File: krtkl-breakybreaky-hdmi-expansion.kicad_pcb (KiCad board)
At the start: 4 copper layers, 62.2 x 19.7 mm, 37 parts, among them J1 SMH-120-02-T-D, J2 685119134923, J3 solder_jumper, Q1 BSS138AKA, Q2 BSS138AKA, Q3 BSS138AKA, U1 TPD12S016PWR, U2 TPS61232DRCT

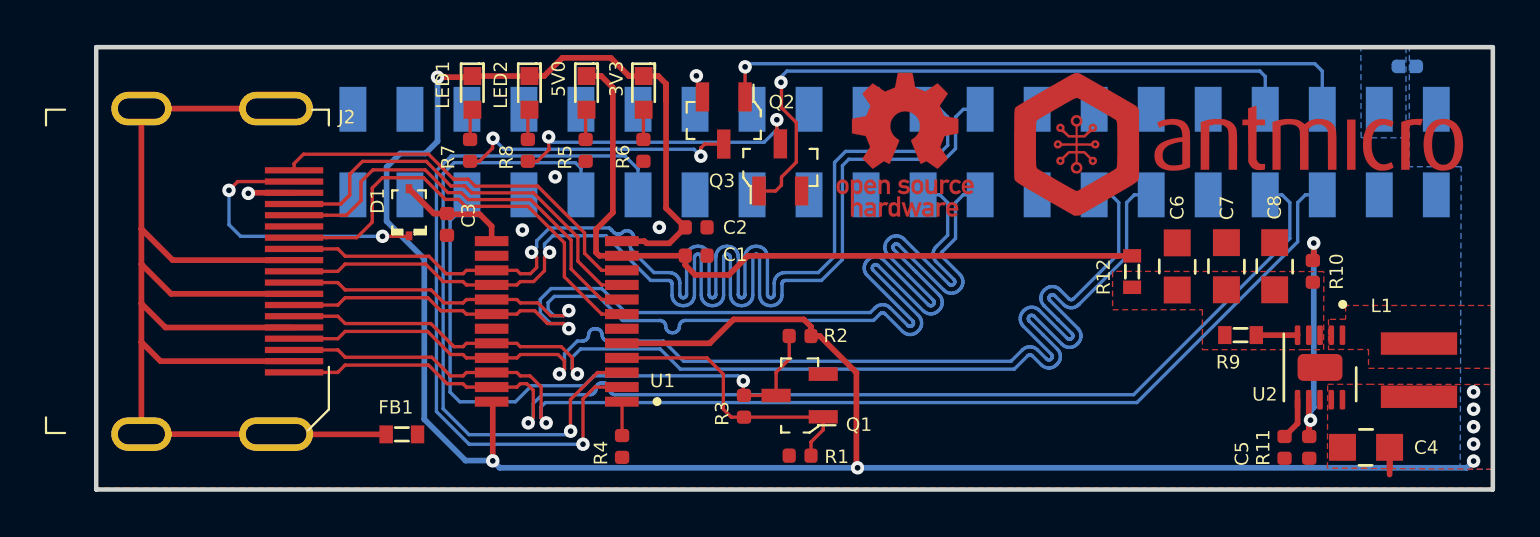
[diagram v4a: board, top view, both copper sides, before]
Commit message: Added testpads, 0R on EDID and board branding to PCB
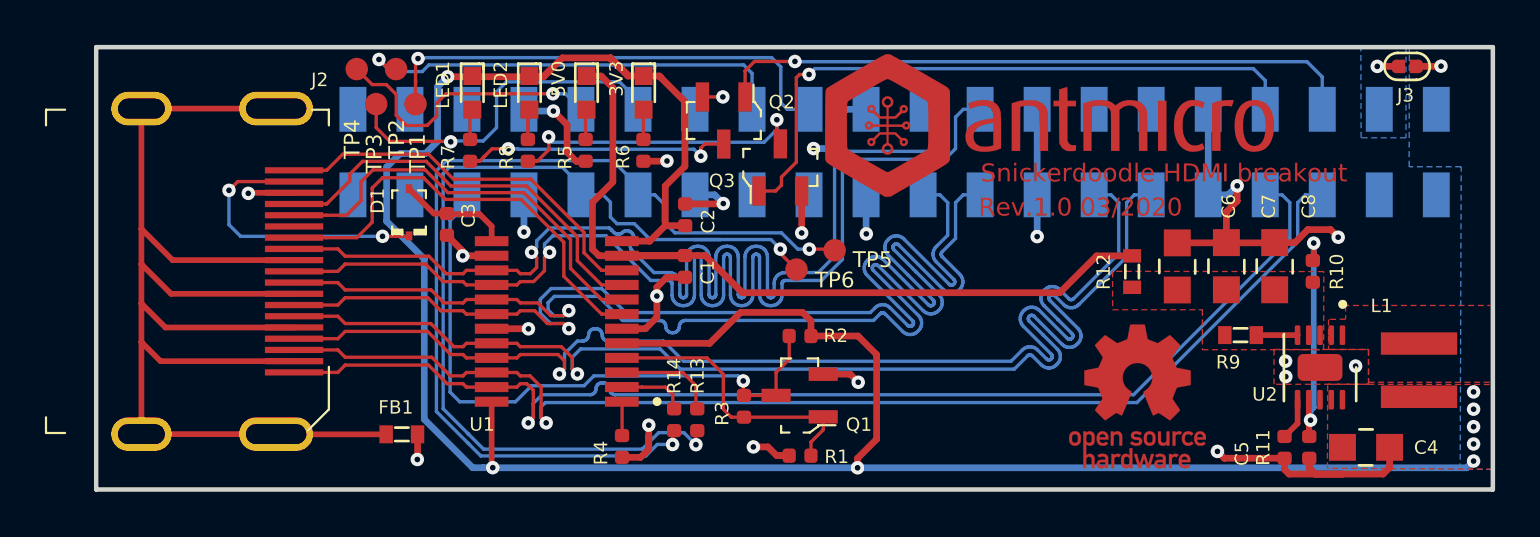
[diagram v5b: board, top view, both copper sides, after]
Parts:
- added R13: R_0R_0402, antmicro-footprints:0402-res, F.Cu at (156.9, 119.1)
- added R14: R_0R_0402, antmicro-footprints:0402-res, F.Cu at (155.9, 119.1)
- added TP1: TP_SMD1MM, antmicro-footprints:Testpoint_smd_1mm, F.Cu at (144.4, 105.1)
- added TP2: TP_SMD1MM, antmicro-footprints:Testpoint_smd_1mm, F.Cu at (143.5, 103.5)
- added TP3: TP_SMD1MM, antmicro-footprints:Testpoint_smd_1mm, F.Cu at (142.6, 105.1)
- added TP4: TP_SMD1MM, antmicro-footprints:Testpoint_smd_1mm, F.Cu at (141.8, 103.5)
- added TP5: TP_SMD1MM, antmicro-footprints:Testpoint_smd_1mm, F.Cu at (163.1, 111.6)
- added TP6: TP_SMD1MM, antmicro-footprints:Testpoint_smd_1mm, F.Cu at (161.4, 112.5)
- 3V3, 5V0, LED1, LED2: footprint antmicro-footprints:LED_0603 -> krtkl-breakybreaky-hdmi-expansion-footprints:LED_0603
- C1, C2, C3, C5: footprint antmicro-footprints:0402-cap -> krtkl-breakybreaky-hdmi-expansion-footprints:0402-cap
- C4, C6, C7, C8: footprint antmicro-footprints:0805-cap -> krtkl-breakybreaky-hdmi-expansion-footprints:0805-cap
- D1: footprint antmicro-footprints:SOD-323F -> krtkl-breakybreaky-hdmi-expansion-footprints:SOD-323F
- FB1, R12, R9: footprint antmicro-footprints:0603-res -> krtkl-breakybreaky-hdmi-expansion-footprints:0603-res
- J1: footprint antmicro-footprints:SMH-120-02-T-D -> krtkl-breakybreaky-hdmi-expansion-footprints:SMH-120-02-T-D
- J2: footprint antmicro-footprints:HDMI_A_Female_685119134923 -> krtkl-breakybreaky-hdmi-expansion-footprints:HDMI_A_Female_685119134923
- J3: footprint antmicro-footprints:SolderJumper-0.6x1.4mm -> krtkl-breakybreaky-hdmi-expansion-footprints:SolderJumper-0.6x1.4mm; moved to F.Cu
- L1: footprint antmicro-footprints:XFL4020-102MEB -> krtkl-breakybreaky-hdmi-expansion-footprints:XFL4020-102MEB
- N1: footprint antmicro-footprints:oshw-logo -> krtkl-breakybreaky-hdmi-expansion-footprints:oshw-logo
- N2: footprint antmicro-footprints:antmicro-logo_scaled_20mm -> krtkl-breakybreaky-hdmi-expansion-footprints:antmicro-logo_scaled_20mm
- Q1, Q2, Q3: footprint antmicro-footprints:SOT-23-3 -> krtkl-breakybreaky-hdmi-expansion-footprints:SOT-23-3
- R1, R10, R11, R2, R3, R4, R5, R6, R7, R8: footprint antmicro-footprints:0402-res -> krtkl-breakybreaky-hdmi-expansion-footprints:0402-res
- U1: footprint antmicro-footprints:TPD12S016PWR -> krtkl-breakybreaky-hdmi-expansion-footprints:TPD12S016PWR
- U2: footprint antmicro-footprints:VSON-10-1EP_3x3mm -> krtkl-breakybreaky-hdmi-expansion-footprints:VSON-10-1EP_3x3mm
- moved N1 15.3 mm to (176.6, 118.1)
- moved N2 8.46 mm to (172.6, 106.2)
- moved C2 0.74 mm to (156.4, 110.0), turned to 270 degrees
- moved C1 0.69 mm to (156.4, 112.3), turned to 90 degrees
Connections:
- U1 pad 2: /HDMI_SCL_3V3 -> Net-(R14-Pad2)
- U1 pad 3: /HDMI_SDA_3V3 -> Net-(R13-Pad2)
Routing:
- net GND: track 4.11 -> 70.7 mm, vias 5 -> 23
- net /IO_L15P_T2_DQS_34: track 0.00 -> 21.6 mm, vias 0 -> 1
- net /IO_L15N_T2_DQS_34: track 0.00 -> 19.7 mm, vias 0 -> 1
- net /IO_L16P_T2_34: track 0.00 -> 15.8 mm, vias 0 -> 1
- net /HDMI_SDA_3V3: track 28.5 -> 43.4 mm, vias 1 -> 2
- net /IO_L16N_T2_34: track 0.00 -> 12.8 mm, vias 0 -> 1
- net /HDMI_SCL_3V3: track 32.5 -> 43.3 mm, vias 1 -> 2
- net 3V3: track 105.8 -> 111.0 mm, vias 8 -> 9
- net Net-(R13-Pad2): track 0.00 -> 4.58 mm
- net 5V0: track 33.9 -> 38.0 mm
- net Net-(R14-Pad2): track 0.00 -> 3.04 mm
- net /GP_LED2: track 29.7 -> 28.7 mm
- net /VCCO_34: track 0.00 -> 0.94 mm, vias 0 -> 1
- net Net-(Q2-Pad3): track 12.8 -> 12.2 mm
- added copper zone on In1.Cu, net GND
- added copper zone on In2.Cu, net GND
- removed copper zone on B.Cu, net GND
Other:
- board text added: "Rev.1.0 03/2020"
- board text added: "Snickerdoodle HDMI breakout"

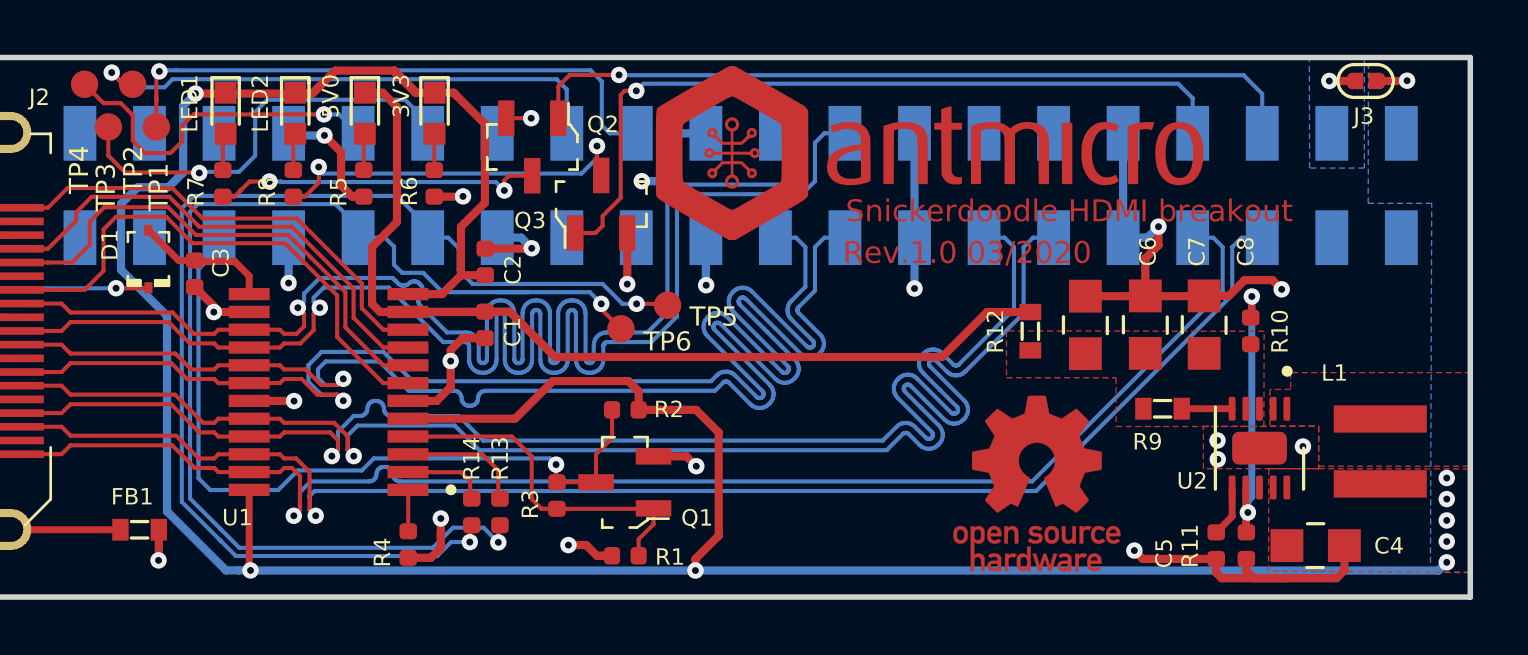
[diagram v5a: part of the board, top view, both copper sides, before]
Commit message: DRC resolved
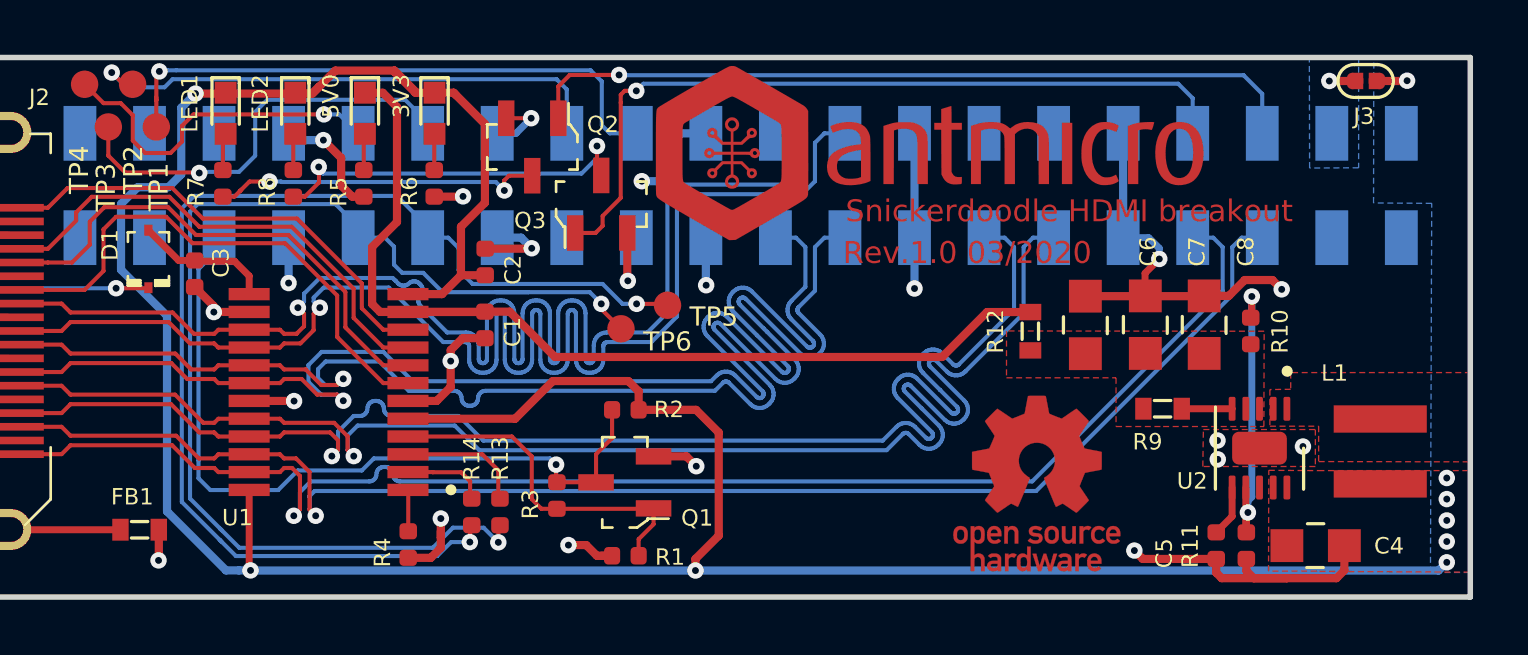
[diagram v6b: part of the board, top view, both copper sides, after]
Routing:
- net GND: track 70.7 -> 71.4 mm

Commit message: Updated documentation, added README and LICENSE
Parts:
- R13, R14: footprint antmicro-footprints:0402-res -> krtkl-breakybreaky-hdmi-expansion-footprints:0402-res
- TP1, TP2, TP3, TP4, TP5, TP6: footprint antmicro-footprints:Testpoint_smd_1mm -> krtkl-breakybreaky-hdmi-expansion-footprints:Testpoint_smd_1mm
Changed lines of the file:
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@@
     (add_net "Net-(U2-Pad8)")
   )
-  (module antmicro-footprints:Testpoint_smd_1mm (layer F.Cu)
+  (module krtkl-breakybreaky-hdmi-expansion-footprints:Testpoint_smd_1mm (layer F.Cu)
     (at 161.36 112.4608)
     (attr virtual)
@@
       (net 34 /HDMI_SDA_3V3))
   )
-  (module antmicro-footprints:Testpoint_smd_1mm (layer F.Cu)
+  (module krtkl-breakybreaky-hdmi-expansion-footprints:Testpoint_smd_1mm (layer F.Cu)
     (at 163.06 111.6008)
     (attr virtual)
@@
       (net 35 /HDMI_SCL_3V3))
   )
-  (module antmicro-footprints:Testpoint_smd_1mm (layer F.Cu)
+  (module krtkl-breakybreaky-hdmi-expansion-footprints:Testpoint_smd_1mm (layer F.Cu)
     (at 141.77 103.5308)
     (attr virtual)
@@
       (net 25 /IO_L16N_T2_34))
   )
-  (module antmicro-footprints:Testpoint_smd_1mm (layer F.Cu)
+  (module krtkl-breakybreaky-hdmi-expansion-footprints:Testpoint_smd_1mm (layer F.Cu)
     (at 142.636666 105.09)
     (attr virtual)
@@
       (net 28 /IO_L16P_T2_34))
   )
-  (module antmicro-footprints:Testpoint_smd_1mm (layer F.Cu)
+  (module krtkl-breakybreaky-hdmi-expansion-footprints:Testpoint_smd_1mm (layer F.Cu)
     (at 143.523332 103.5308)
     (attr virtual)
@@
       (net 23 /IO_L15N_T2_DQS_34))
   )
-  (module antmicro-footprints:Testpoint_smd_1mm (layer F.Cu)
+  (module krtkl-breakybreaky-hdmi-expansion-footprints:Testpoint_smd_1mm (layer F.Cu)
     (at 144.389998 105.09)
     (attr virtual)
@@
       (net 27 /IO_L15P_T2_DQS_34))
   )
-  (module antmicro-footprints:0402-res (layer F.Cu)
+  (module krtkl-breakybreaky-hdmi-expansion-footprints:0402-res (layer F.Cu)
     (at 155.91 119.1 90)
     (descr "Resistor SMD 0402 (1005 Metric), square (rectangular) end terminal, IPC_7351 nominal, (Body size source: http://www.tortai-tech.com/upload/download/2011102023233369053.pdf), generated with kicad-footprint-generator")
@@
     (pad 1 smd roundrect (at -0.485 0 90) (size 0.59 0.64) (layers F.Cu F.Paste F.Mask) (roundrect_rratio 0.25)
       (net 35 /HDMI_SCL_3V3))
-    (model ${ANT3DMDL}/0402-res.step
+    (model ${KIPRJMOD}/lib/3d-models/0402-res.step
       (offset (xyz 0 0 -0.01))
       (scale (xyz 1 1 1))
@@
     )
   )
-  (module antmicro-footprints:0402-res (layer F.Cu)
+  (module krtkl-breakybreaky-hdmi-expansion-footprints:0402-res (layer F.Cu)
     (at 156.94 119.1 90)
     (descr "Resistor SMD 0402 (1005 Metric), square (rectangular) end terminal, IPC_7351 nominal, (Body size source: http://www.tortai-tech.com/upload/download/2011102023233369053.pdf), generated with kicad-footprint-generator")
@@
     (pad 1 smd roundrect (at -0.485 0 90) (size 0.59 0.64) (layers F.Cu F.Paste F.Mask) (roundrect_rratio 0.25)
       (net 34 /HDMI_SDA_3V3))
-    (model ${ANT3DMDL}/0402-res.step
+    (model ${KIPRJMOD}/lib/3d-models/0402-res.step
       (offset (xyz 0 0 -0.01))
       (scale (xyz 1 1 1))
